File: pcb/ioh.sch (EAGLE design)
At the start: 27 parts, among them Q1 MOSFET-NCHANNEL2N7000, Q2 MOSFET-NCHANNEL2N7000, Q3 MOSFET-NCHANNEL2N7000, Q4 MOSFET-NCHANNEL2N7000

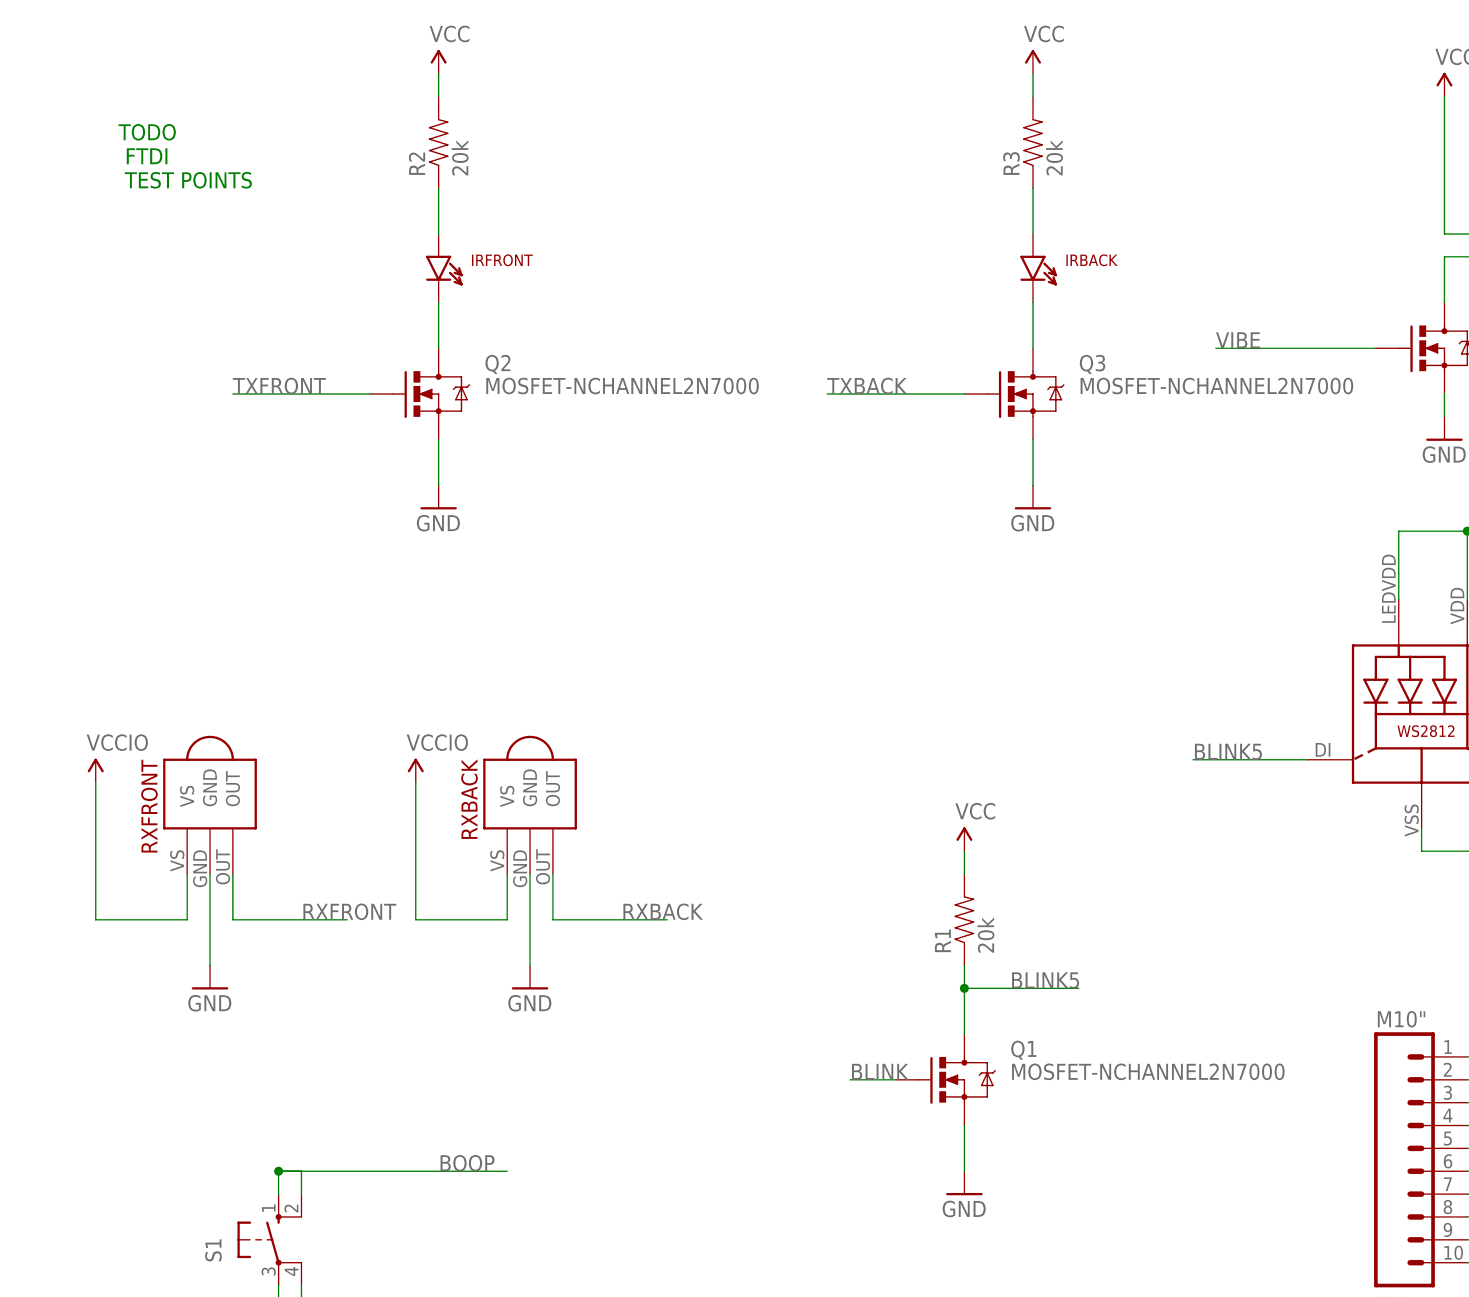
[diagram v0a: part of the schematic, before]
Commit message: solder jumpers
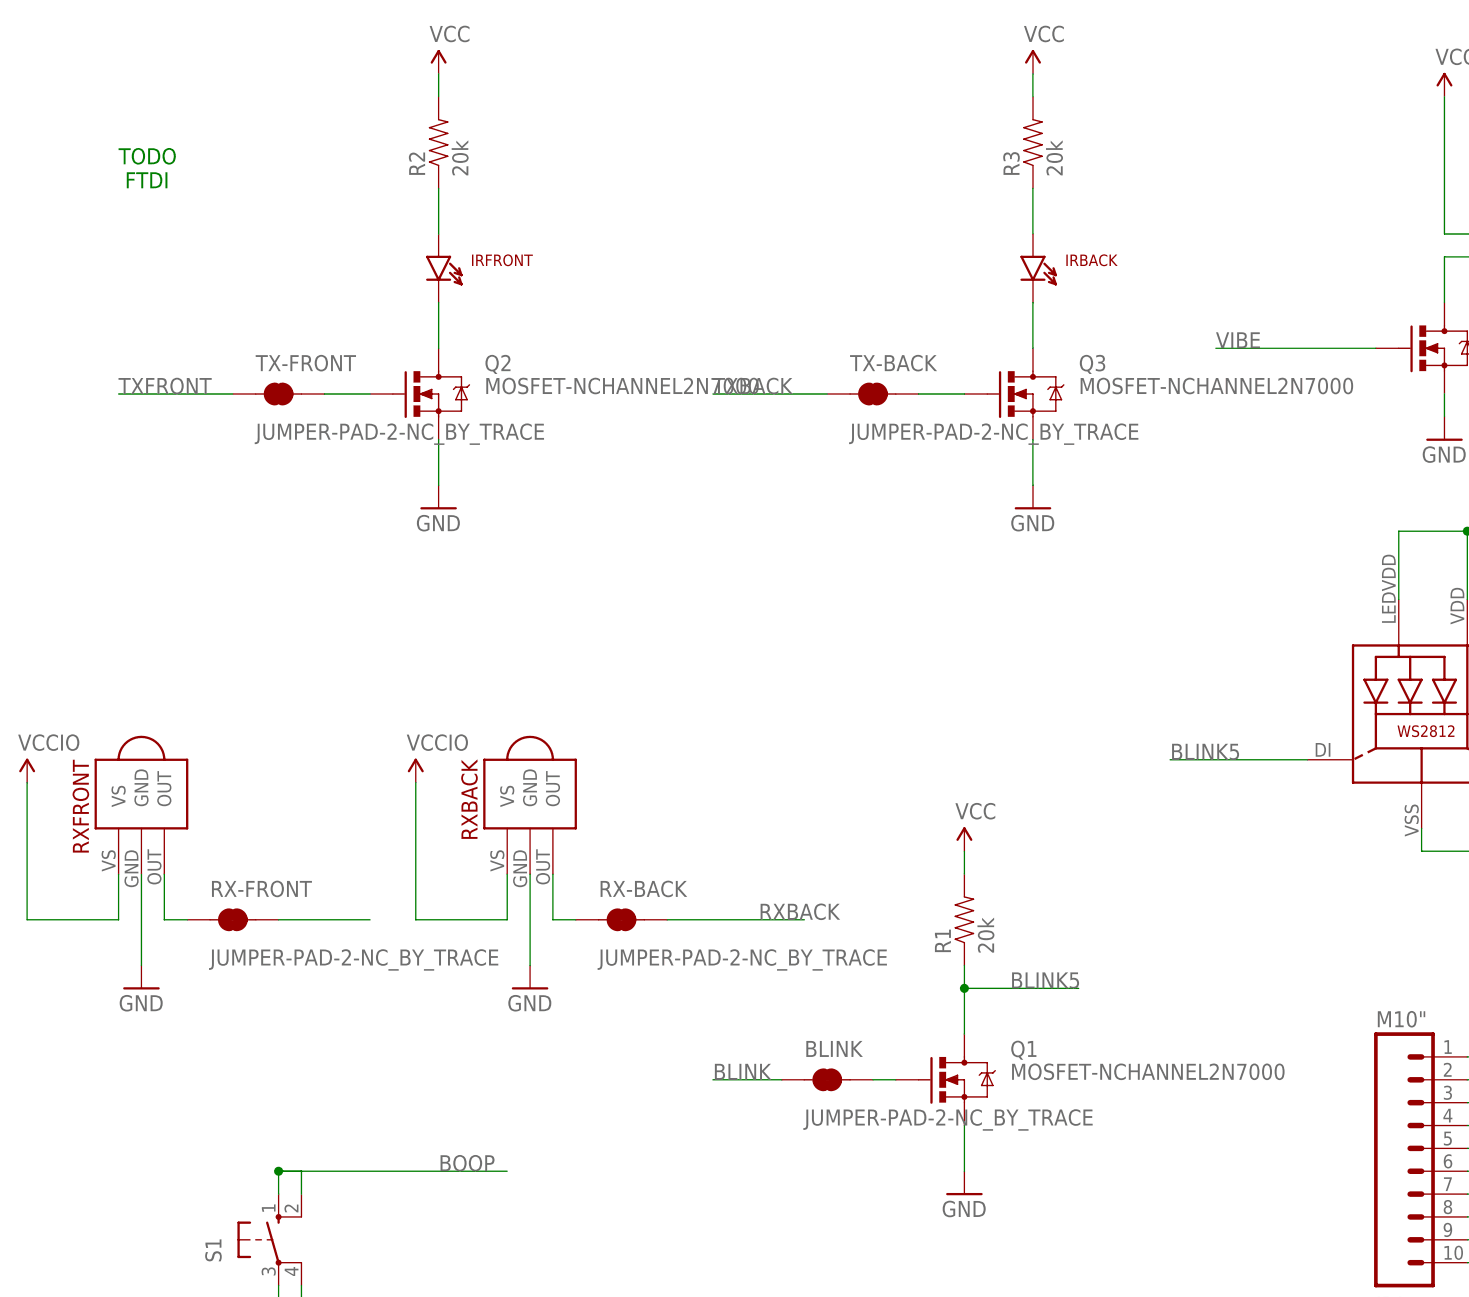
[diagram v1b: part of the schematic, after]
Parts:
- added BLINK, RX-BACK, RX-FRONT, TX-BACK, TX-FRONT: JUMPER-PAD-2-NC_BY_TRACE, SparkFun-Passives:JUMPER-PAD-2-NC_BY_TRACE
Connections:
- new net N$15: RX-BACK.1, RXBACK.OUT
- new net N$17: RX-FRONT.1, RXFRONT.OUT
- new net N$20: Q2.G, TX-FRONT.2
- new net N$21: Q3.G, TX-BACK.2
- new net N$6: BLINK.2, Q1.G
- net BLINK: now also BLINK.1; no longer Q1.G
- net RXBACK: now also RX-BACK.2; no longer RXBACK.OUT
- net RXFRONT: now also RX-FRONT.2; no longer RXFRONT.OUT
- net TXBACK: now also TX-BACK.1; no longer Q3.G
- net TXFRONT: now also TX-FRONT.1; no longer Q2.G
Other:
- note added: "TODO FTDI"
- note removed: "TODO FTDI TEST POINTS"
- moved on the sheet: RXFRONT
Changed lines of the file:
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@@
 <part name="GND" library="SparkFun-Connectors" deviceset="M01" device="PTH"/>
 <part name="LOGO1" library="SparkFun-Aesthetics" deviceset="OSHW-LOGO" device="S"/>
+<part name="BLINK" library="SparkFun-Passives" deviceset="JUMPER-PAD-2-NC_BY_TRACE" device=""/>
+<part name="RX-BACK" library="SparkFun-Passives" deviceset="JUMPER-PAD-2-NC_BY_TRACE" device=""/>
+<part name="RX-FRONT" library="SparkFun-Passives" deviceset="JUMPER-PAD-2-NC_BY_TRACE" device=""/>
+<part name="TX-BACK" library="SparkFun-Passives" deviceset="JUMPER-PAD-2-NC_BY_TRACE" device=""/>
+<part name="TX-FRONT" library="SparkFun-Passives" deviceset="JUMPER-PAD-2-NC_BY_TRACE" device=""/>
 </parts>
 <sheets>
@@
 <plain>
 <text x="-132.08" y="180.34" size="1.778" layer="91">TODO
- FTDI
- TEST POINTS</text>
+ FTDI</text>
 </plain>
 <instances>
@@
 <instance part="Q3" gate="G$1" x="-30.48" y="157.48"/>
 <instance part="GND6" gate="1" x="-30.48" y="144.78"/>
-<instance part="RXFRONT" gate="G$1" x="-121.92" y="116.84" rot="R270"/>
-<instance part="GND7" gate="1" x="-121.92" y="91.44"/>
-<instance part="SUPPLY8" gate="G$1" x="-134.62" y="114.3"/>
+<instance part="RXFRONT" gate="G$1" x="-129.54" y="116.84" rot="R270"/>
+<instance part="GND7" gate="1" x="-129.54" y="91.44"/>
+<instance part="SUPPLY8" gate="G$1" x="-142.24" y="114.3"/>
 <instance part="RXBACK" gate="G$1" x="-86.36" y="116.84" rot="R270"/>
 <instance part="GND8" gate="1" x="-86.36" y="91.44"/>
@@
 <instance part="GND" gate="G$1" x="154.94" y="45.72" rot="R180"/>
 <instance part="LOGO1" gate="G$1" x="-58.42" y="48.26"/>
+<instance part="BLINK" gate="G$1" x="-53.34" y="81.28"/>
+<instance part="RX-BACK" gate="G$1" x="-76.2" y="99.06"/>
+<instance part="RX-FRONT" gate="G$1" x="-119.38" y="99.06"/>
+<instance part="TX-BACK" gate="G$1" x="-48.26" y="157.48"/>
+<instance part="TX-FRONT" gate="G$1" x="-114.3" y="157.48"/>
 </instances>
 <busses>
@@
 <pinref part="RXFRONT" gate="G$1" pin="GND"/>
 <pinref part="GND7" gate="1" pin="GND"/>
-<wire x1="-121.92" y1="104.14" x2="-121.92" y2="93.98" width="0.1524" layer="91"/>
+<wire x1="-129.54" y1="104.14" x2="-129.54" y2="93.98" width="0.1524" layer="91"/>
 </segment>
 <segment>
@@
 <segment>
 <pinref part="SUPPLY8" gate="G$1" pin="VCCIO"/>
-<wire x1="-134.62" y1="114.3" x2="-134.62" y2="99.06" width="0.1524" layer="91"/>
-<wire x1="-134.62" y1="99.06" x2="-124.46" y2="99.06" width="0.1524" layer="91"/>
+<wire x1="-142.24" y1="114.3" x2="-142.24" y2="99.06" width="0.1524" layer="91"/>
+<wire x1="-142.24" y1="99.06" x2="-132.08" y2="99.06" width="0.1524" layer="91"/>
 <pinref part="RXFRONT" gate="G$1" pin="VS"/>
-<wire x1="-124.46" y1="99.06" x2="-124.46" y2="104.14" width="0.1524" layer="91"/>
+<wire x1="-132.08" y1="99.06" x2="-132.08" y2="104.14" width="0.1524" layer="91"/>
 </segment>
 <segment>
@@
 </segment>
 <segment>
-<pinref part="Q1" gate="G$1" pin="G"/>
-<wire x1="-45.72" y1="81.28" x2="-50.8" y2="81.28" width="0.1524" layer="91"/>
-<label x="-50.8" y="81.28" size="1.778" layer="95"/>
+<pinref part="BLINK" gate="G$1" pin="1"/>
+<wire x1="-58.42" y1="81.28" x2="-66.04" y2="81.28" width="0.1524" layer="91"/>
+<label x="-66.04" y="81.28" size="1.778" layer="95"/>
 </segment>
 </net>
 <net name="BLINK5" class="0">
-<segment>
-<pinref part="LED2" gate="G$1" pin="DI"/>
-<wire x1="0" y1="116.84" x2="-12.7" y2="116.84" width="0.1524" layer="91"/>
-<label x="-12.7" y="116.84" size="1.778" layer="95"/>
-</segment>
 <segment>
 <pinref part="R1" gate="G$1" pin="1"/>
@@
 <label x="-33.02" y="91.44" size="1.778" layer="95"/>
 </segment>
+<segment>
+<pinref part="LED2" gate="G$1" pin="DI"/>
+<wire x1="0" y1="116.84" x2="-15.24" y2="116.84" width="0.1524" layer="91"/>
+<label x="-15.24" y="116.84" size="1.778" layer="95"/>
+</segment>
 </net>
 <net name="N$4" class="0">
@@
 </net>
 <net name="TXBACK" class="0">
-<segment>
-<pinref part="Q3" gate="G$1" pin="G"/>
-<wire x1="-38.1" y1="157.48" x2="-53.34" y2="157.48" width="0.1524" layer="91"/>
-<label x="-53.34" y="157.48" size="1.778" layer="95"/>
-</segment>
 <segment>
 <pinref part="U$1" gate="G$1" pin="AD4"/>
@@
 <label x="68.58" y="76.2" size="1.778" layer="95"/>
 </segment>
+<segment>
+<pinref part="TX-BACK" gate="G$1" pin="1"/>
+<wire x1="-53.34" y1="157.48" x2="-66.04" y2="157.48" width="0.1524" layer="91"/>
+<label x="-66.04" y="157.48" size="1.778" layer="95"/>
+</segment>
 </net>
 <net name="N$24" class="0">
@@
 </net>
 <net name="TXFRONT" class="0">
-<segment>
-<pinref part="Q2" gate="G$1" pin="G"/>
-<wire x1="-104.14" y1="157.48" x2="-119.38" y2="157.48" width="0.1524" layer="91"/>
-<label x="-119.38" y="157.48" size="1.778" layer="95"/>
-</segment>
 <segment>
 <pinref part="U$1" gate="G$1" pin="AD3"/>
@@
 <label x="68.58" y="78.74" size="1.778" layer="95"/>
 </segment>
+<segment>
+<pinref part="TX-FRONT" gate="G$1" pin="1"/>
+<wire x1="-119.38" y1="157.48" x2="-132.08" y2="157.48" width="0.1524" layer="91"/>
+<label x="-132.08" y="157.48" size="1.778" layer="95"/>
+</segment>
 </net>
 <net name="RXFRONT" class="0">
-<segment>
-<pinref part="RXFRONT" gate="G$1" pin="OUT"/>
-<wire x1="-119.38" y1="104.14" x2="-119.38" y2="99.06" width="0.1524" layer="91"/>
-<wire x1="-119.38" y1="99.06" x2="-106.68" y2="99.06" width="0.1524" layer="91"/>
-<label x="-111.76" y="99.06" size="1.778" layer="95"/>
-</segment>
 <segment>
 <pinref part="JP1" gate="G$1" pin="3"/>
@@
 <label x="17.78" y="78.74" size="1.778" layer="95"/>
 </segment>
+<segment>
+<pinref part="RX-FRONT" gate="G$1" pin="2"/>
+<wire x1="-114.3" y1="99.06" x2="-104.14" y2="99.06" width="0.1524" layer="91"/>
+</segment>
 </net>
 <net name="RXBACK" class="0">
-<segment>
-<pinref part="RXBACK" gate="G$1" pin="OUT"/>
-<wire x1="-83.82" y1="104.14" x2="-83.82" y2="99.06" width="0.1524" layer="91"/>
-<wire x1="-83.82" y1="99.06" x2="-71.12" y2="99.06" width="0.1524" layer="91"/>
-<label x="-76.2" y="99.06" size="1.778" layer="95"/>
-</segment>
 <segment>
 <pinref part="U$1" gate="G$1" pin="RX0"/>
@@
 <wire x1="68.58" y1="68.58" x2="81.28" y2="68.58" width="0.1524" layer="91"/>
 <label x="68.58" y="68.58" size="1.778" layer="95"/>
+</segment>
+<segment>
+<pinref part="RX-BACK" gate="G$1" pin="2"/>
+<wire x1="-71.12" y1="99.06" x2="-55.88" y2="99.06" width="0.1524" layer="91"/>
+<label x="-60.96" y="99.06" size="1.778" layer="95"/>
 </segment>
 </net>
@@
 </segment>
 </net>
+<net name="N$6" class="0">
+<segment>
+<pinref part="Q1" gate="G$1" pin="G"/>
+<pinref part="BLINK" gate="G$1" pin="2"/>
+<wire x1="-45.72" y1="81.28" x2="-48.26" y2="81.28" width="0.1524" layer="91"/>
+</segment>
+</net>
+<net name="N$15" class="0">
+<segment>
+<pinref part="RXBACK" gate="G$1" pin="OUT"/>
+<wire x1="-83.82" y1="104.14" x2="-83.82" y2="99.06" width="0.1524" layer="91"/>
+<pinref part="RX-BACK" gate="G$1" pin="1"/>
+<wire x1="-83.82" y1="99.06" x2="-81.28" y2="99.06" width="0.1524" layer="91"/>
+</segment>
+</net>
+<net name="N$17" class="0">
+<segment>
+<pinref part="RXFRONT" gate="G$1" pin="OUT"/>
+<wire x1="-127" y1="104.14" x2="-127" y2="99.06" width="0.1524" layer="91"/>
+<pinref part="RX-FRONT" gate="G$1" pin="1"/>
+<wire x1="-127" y1="99.06" x2="-124.46" y2="99.06" width="0.1524" layer="91"/>
+</segment>
+</net>
+<net name="N$20" class="0">
+<segment>
+<pinref part="TX-FRONT" gate="G$1" pin="2"/>
+<pinref part="Q2" gate="G$1" pin="G"/>
+<wire x1="-109.22" y1="157.48" x2="-104.14" y2="157.48" width="0.1524" layer="91"/>
+</segment>
+</net>
+<net name="N$21" class="0">
+<segment>
+<pinref part="TX-BACK" gate="G$1" pin="2"/>
+<pinref part="Q3" gate="G$1" pin="G"/>
+<wire x1="-43.18" y1="157.48" x2="-38.1" y2="157.48" width="0.1524" layer="91"/>
+</segment>
+</net>
